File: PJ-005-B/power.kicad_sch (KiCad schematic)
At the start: 38 parts, among them J1 2 Pin JST XH, J10 Conn_01x03_Pin, U1 MIC29302WU-TR, U2 MIC29302WU-TR, U3 MIC29302WU-TR, U4 LM337IMP/NOPB, U6 MIC5365-2.5YC5-TR

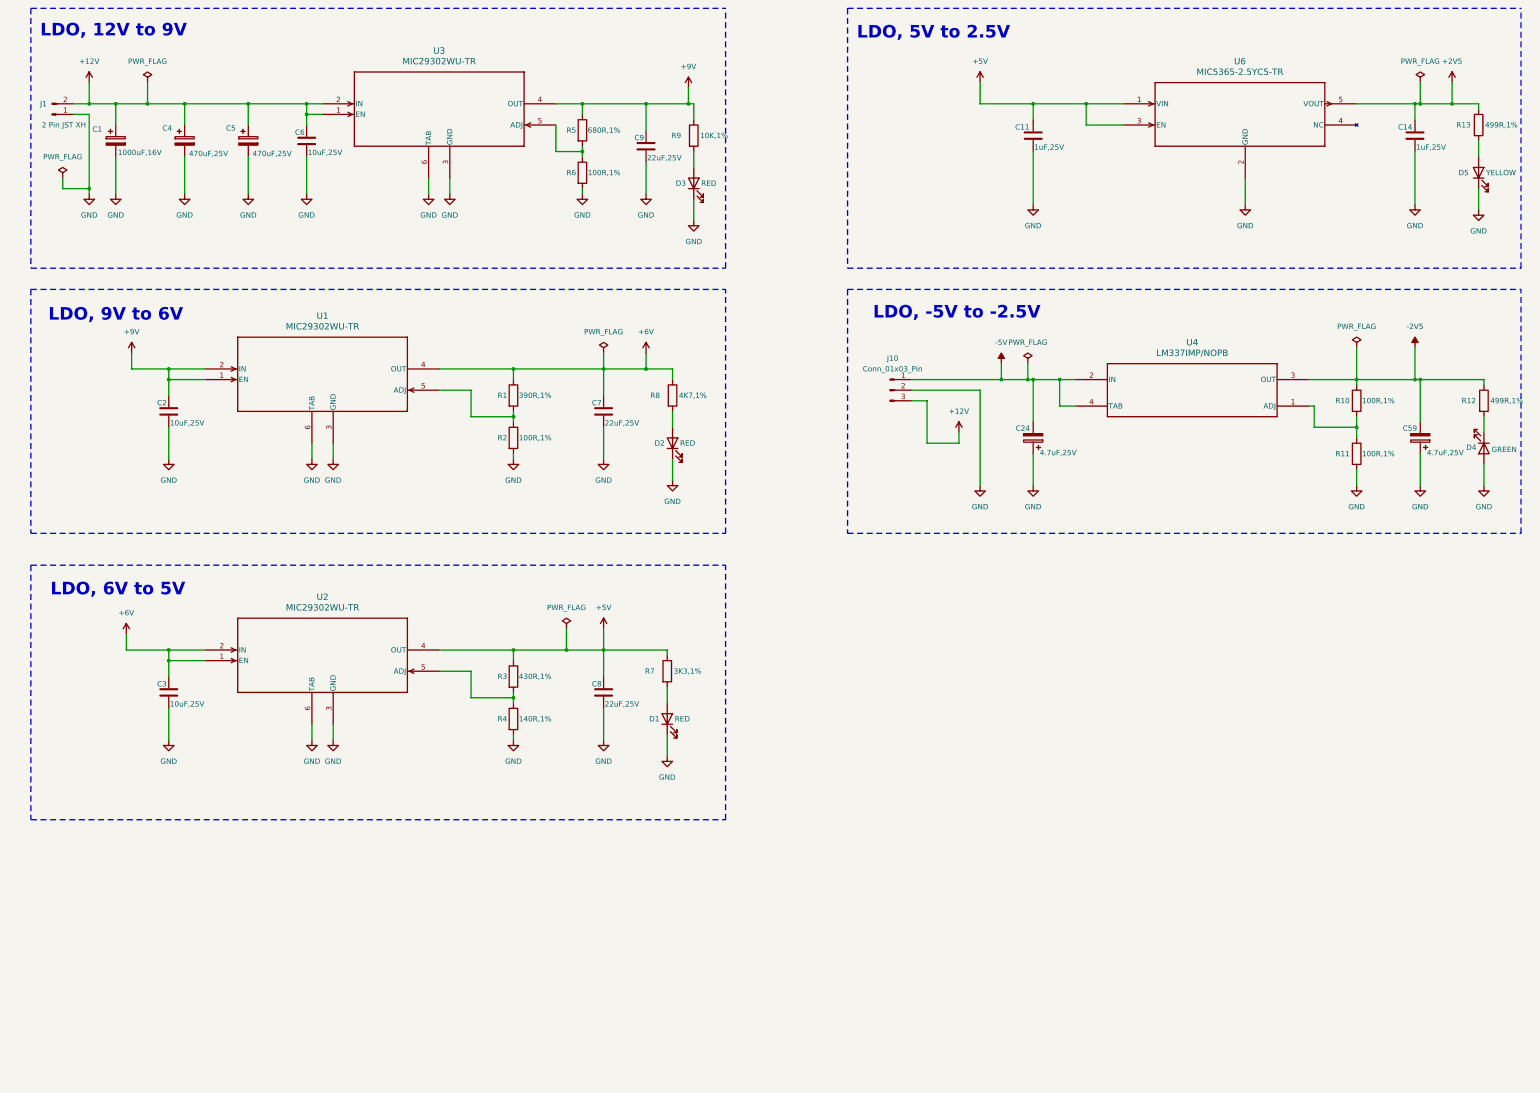
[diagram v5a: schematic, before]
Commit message: Removed filter, inverting amplifiers, buffer and PGA
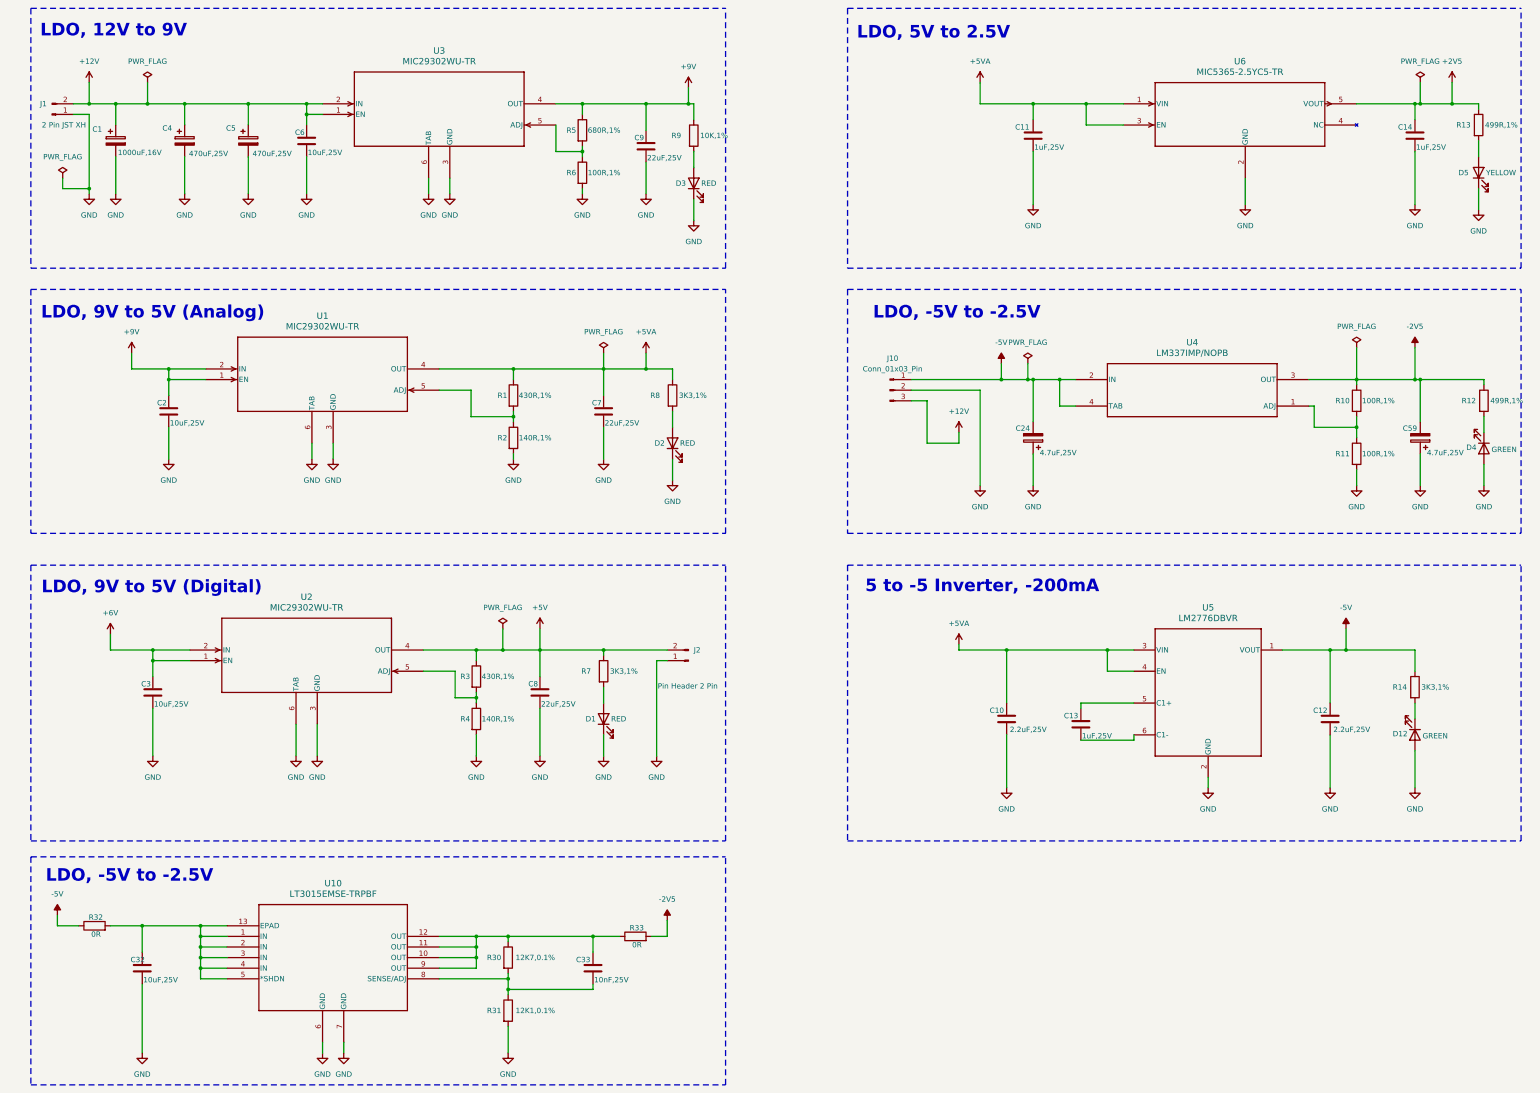
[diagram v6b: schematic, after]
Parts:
- added C10, C12: 2.2uF,25V, XaltenFootprints:C0603, symbol Device:C
- added C13: 1uF,25V, XaltenFootprints:C0603, symbol Device:C
- added C32: 10uF,25V, XaltenFootprints:C0603, symbol Device:C
- added C33: 10nF,25V, XaltenFootprints:C0603, symbol Device:C
- added D12: GREEN, LED_SMD:LED_0603_1608Metric, symbol Device:LED
- added J2: Pin Header 2 Pin, Connector_PinHeader_2.54mm:PinHeader_1x02_P2.54mm_Vertical, symbol Connector:Conn_01x02_Pin
- added R14: 3K3,1%, XaltenFootprints:R0603, symbol Device:R
- added R30: 12K7,0.1%, XaltenFootprints:R0603, symbol Device:R
- added R31: 12K1,0.1%, XaltenFootprints:R0603, symbol Device:R
- added R32, R33: 0R, XaltenFootprints:R0603, symbol Device:R
- added U10: LT3015EMSE-TRPBF, Echosounder Transceiver FP:MSOP-12, symbol Echosounder Transceiver:LT3015EMSE-TRPBF
- added U5: LM2776DBVR, Echosounder Transceiver FP:SOT23-6, symbol Echosounder Transceiver:LM2776DBVR
- R1: value 390R,1% -> 430R,1%
- R2: value 100R,1% -> 140R,1%
- R8: value 4K7,1% -> 3K3,1%
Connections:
- net +5V: now also J2.2 (Pin_2); no longer C11.1, U6.1 (VIN), U6.3 (EN)
- net +6V: no longer C7.1, R1.1, R8.1, U1.4 (OUT)
- net -2V5: now also R33.2
- net -5V: now also C12.1, R14.1, R32.1, U5.1 (VOUT)
- net GND: now also C10.2, C12.2, C32.2, D12.2 (A), J2.1 (Pin_1), R31.2, U10.6 (GND), U10.7 (GND), U5.2 (GND)
- new net: C33.1, R30.1, R33.1, U10.10 (OUT), U10.11 (OUT), U10.12 (OUT), U10.9 (OUT)
- new net: C33.2, R30.2, R31.1, U10.8 (SENSE/ADJ)
- new net: C32.1, R32.2, U10.1 (IN), U10.13 (EPAD), U10.2 (IN), U10.3 (IN), U10.4 (IN), U10.5 (*SHDN)
- new net: D12.1 (K), R14.2
- new net: C13.1, U5.5 (C1+)
- new net: C13.2, U5.6 (C1-)
- new net +5VA: C10.1, C11.1, C7.1, R1.1, R8.1, U1.4 (OUT), U5.3 (VIN), U5.4 (EN), U6.1 (VIN), U6.3 (EN)
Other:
- note added: "5 to -5 Inverter, -200mA"
- note added: "LDO, 9V to 5V (Analog)"
- note added: "LDO, 9V to 5V (Digital)"
- note removed: "LDO, 6V to 5V"
- note removed: "LDO, 9V to 6V"
- moved on the sheet: C3, C8, D1, R3, R4, R7, U2
